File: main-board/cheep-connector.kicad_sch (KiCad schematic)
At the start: 5 parts, among them J1 Conn_02x16_Odd_Even, J2 Conn_02x16_Odd_Even, J3 Conn_02x16_Odd_Even, J4 Conn_02x16_Odd_Even, J5 Conn_02x16_Odd_Even

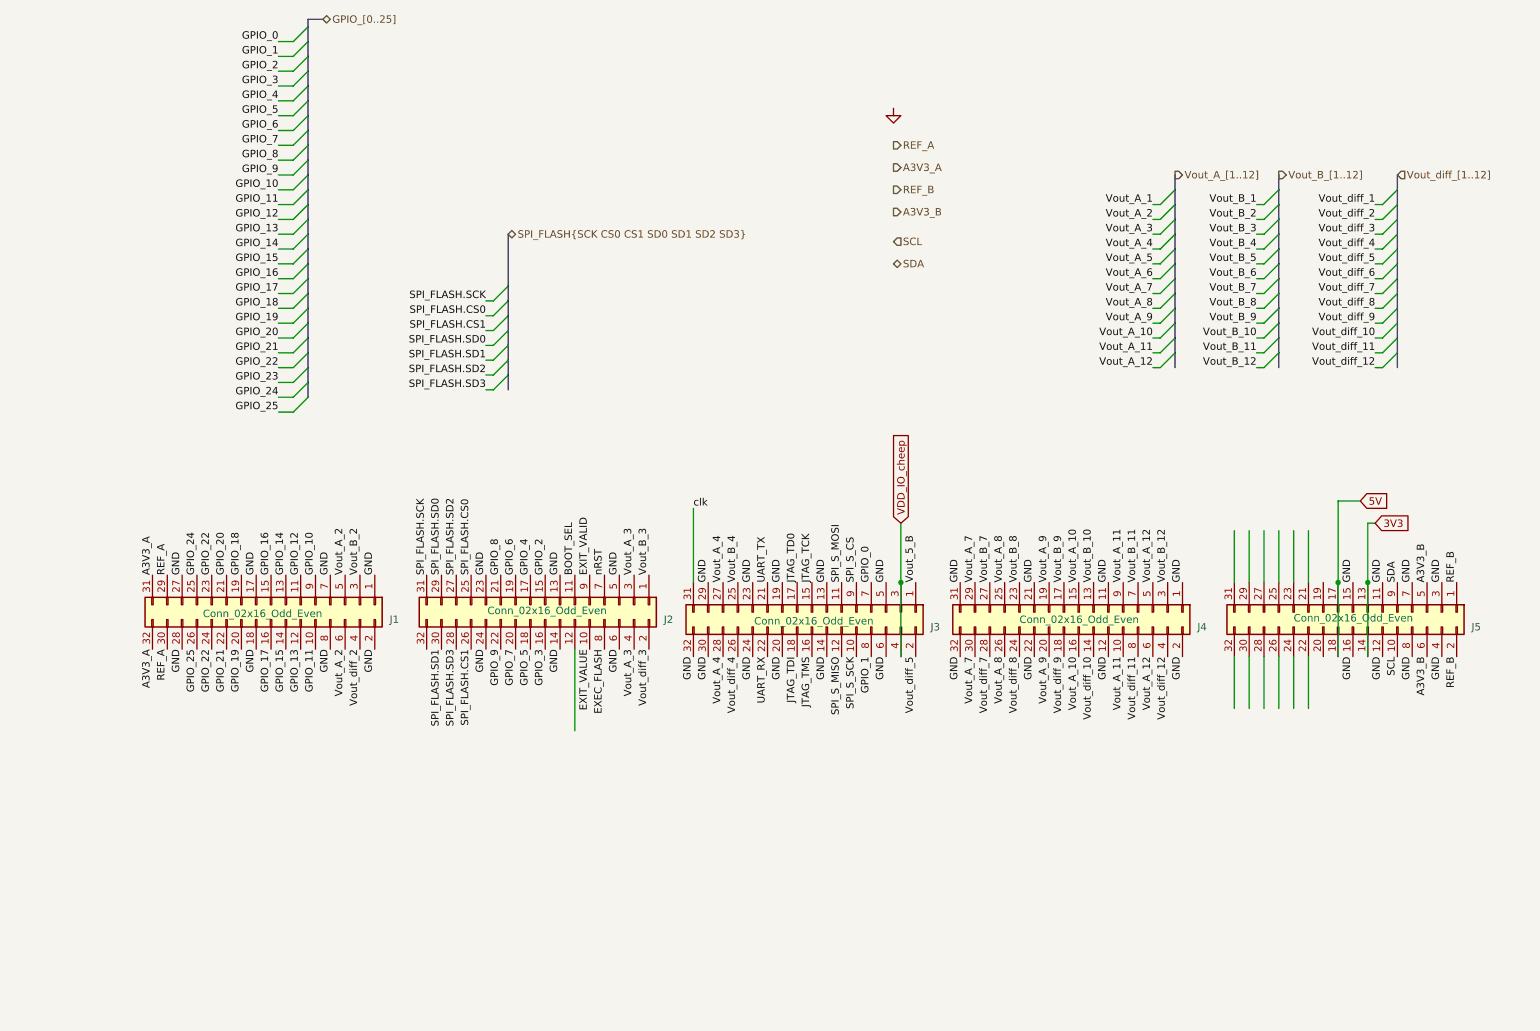
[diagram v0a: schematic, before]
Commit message: WIP: added i2c expanders and re-structuring i2c distributino
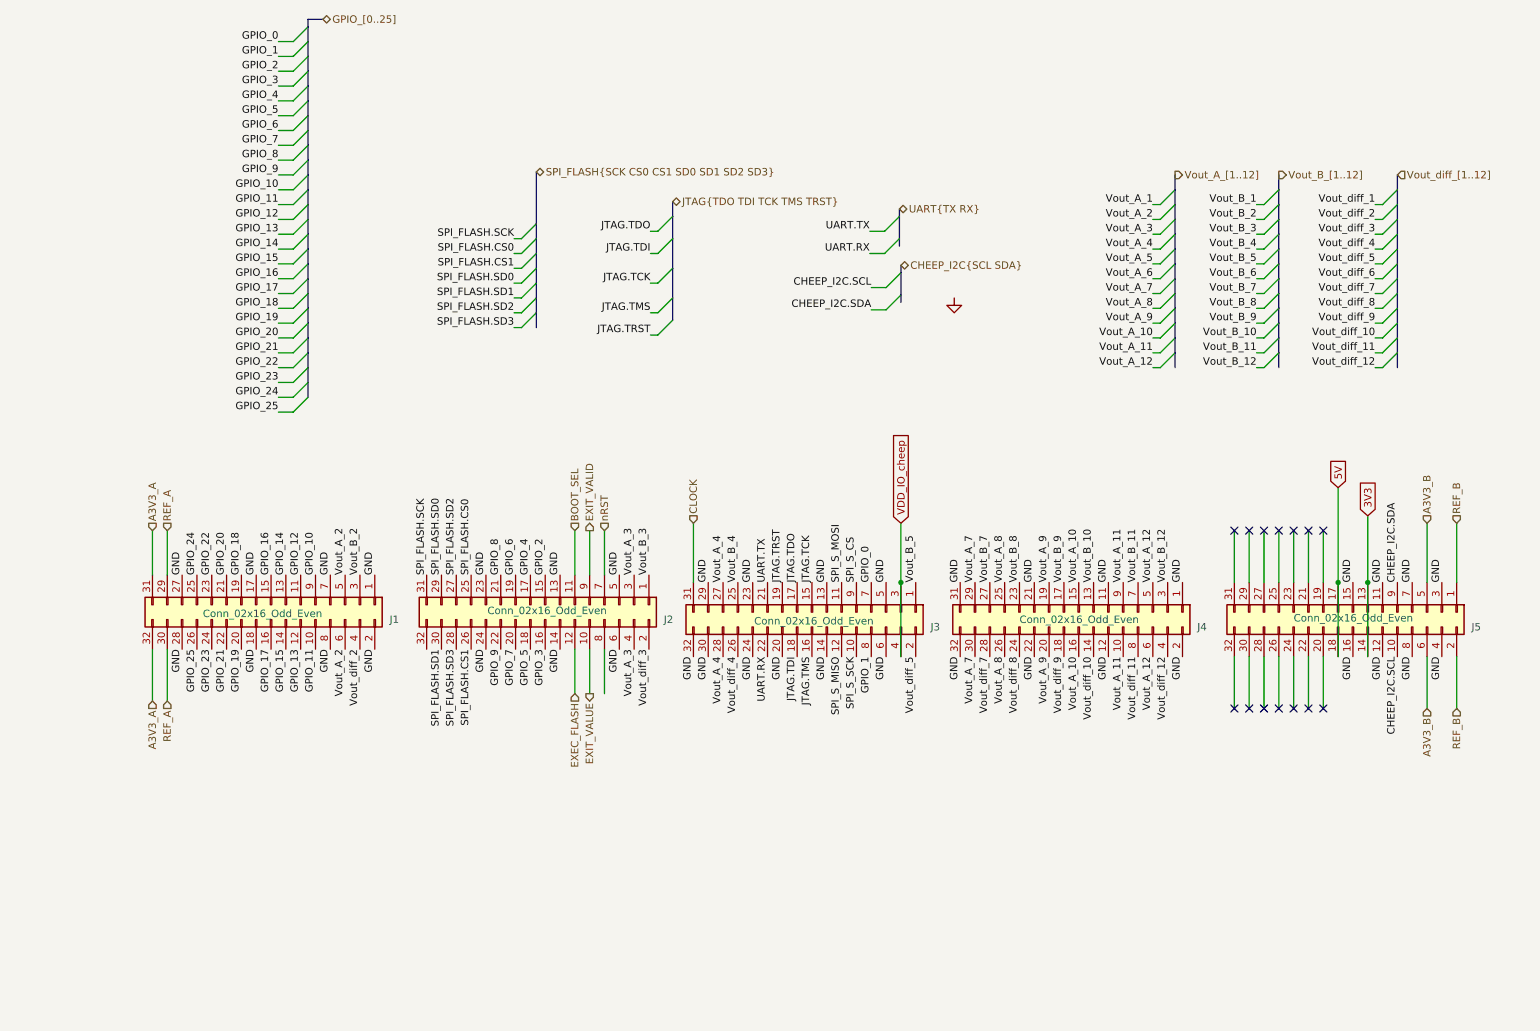
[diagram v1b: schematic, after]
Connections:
- net Vout_5_B is gone; now on net Vout_B_5: J3.1 (Pin_1)
- net EXEC_FLASH: now also J2.12 (Pin_12); no longer J2.8 (Pin_8)
- net GND: no longer J3.19 (Pin_19)
- net GPIO_22: no longer J1.24 (Pin_24)
- net GPIO_23: now also J1.24 (Pin_24)
- net JTAG_TCK renamed JTAG.TCK
- net JTAG_TD0 renamed JTAG.TDO
- net JTAG_TDI renamed JTAG.TDI
- net JTAG_TMS renamed JTAG.TMS
- net SCL renamed CHEEP_I2C.SCL
- net SDA renamed CHEEP_I2C.SDA
- net UART_RX renamed UART.RX
- net UART_TX renamed UART.TX
- net clk renamed CLOCK
- new net JTAG.TRST: J3.19 (Pin_19)
- no-connect marks 0 -> 14

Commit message: Routed all power signals and re-organized GPIOs
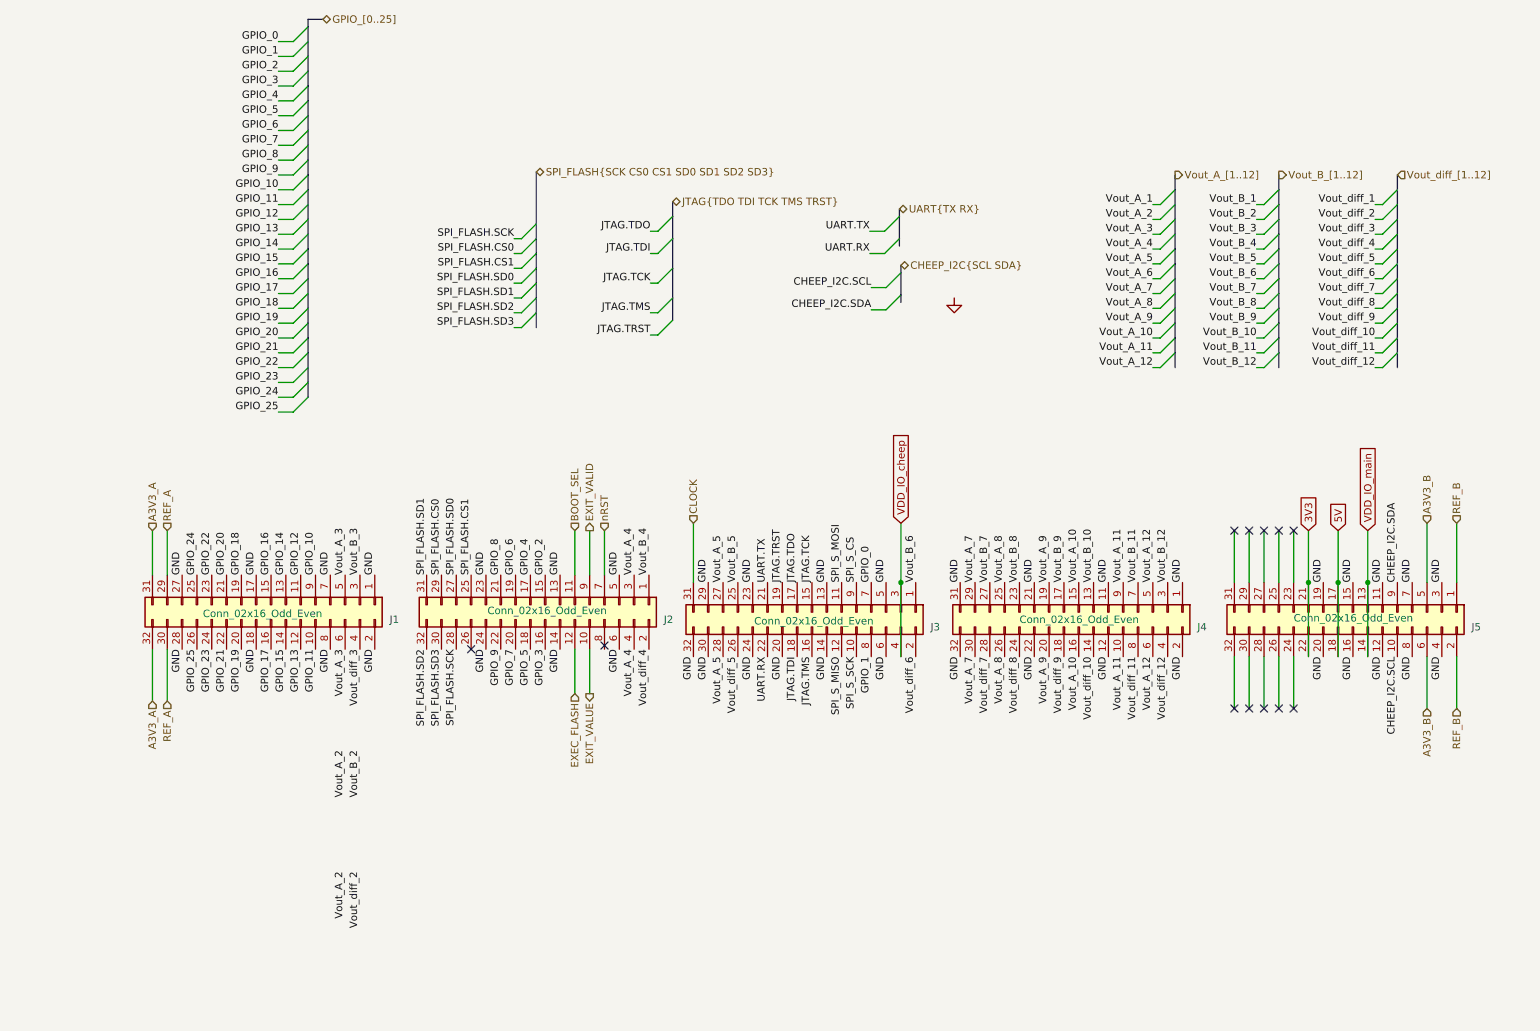
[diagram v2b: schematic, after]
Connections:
- net 3V3: now also J5.21 (Pin_21), J5.22 (Pin_22); no longer J5.13 (Pin_13), J5.14 (Pin_14)
- net GND: now also J5.19 (Pin_19), J5.20 (Pin_20)
- net SPI_FLASH.CS0: now also J2.29 (Pin_29); no longer J2.25 (Pin_25)
- net SPI_FLASH.CS1: now also J2.25 (Pin_25); no longer J2.26 (Pin_26)
- net SPI_FLASH.SCK: now also J2.28 (Pin_28); no longer J2.31 (Pin_31)
- net SPI_FLASH.SD0: now also J2.27 (Pin_27); no longer J2.29 (Pin_29)
- net SPI_FLASH.SD1: now also J2.31 (Pin_31); no longer J2.30 (Pin_30)
- net SPI_FLASH.SD2: now also J2.32 (Pin_32); no longer J2.27 (Pin_27)
- net SPI_FLASH.SD3: now also J2.30 (Pin_30); no longer J2.28 (Pin_28)
- net Vout_A_2: no longer J1.5 (Pin_5), J1.6 (Pin_6)
- net Vout_A_3: now also J1.5 (Pin_5), J1.6 (Pin_6); no longer J2.3 (Pin_3), J2.4 (Pin_4)
- net Vout_A_4: now also J2.3 (Pin_3), J2.4 (Pin_4); no longer J3.27 (Pin_27), J3.28 (Pin_28)
- net Vout_A_5: now also J3.27 (Pin_27), J3.28 (Pin_28)
- net Vout_B_2: no longer J1.3 (Pin_3)
- net Vout_B_3: now also J1.3 (Pin_3); no longer J2.1 (Pin_1)
- net Vout_B_4: now also J2.1 (Pin_1); no longer J3.25 (Pin_25)
- net Vout_B_5: now also J3.25 (Pin_25); no longer J3.1 (Pin_1)
- net Vout_B_6: now also J3.1 (Pin_1)
- net Vout_diff_2: no longer J1.4 (Pin_4)
- net Vout_diff_3: now also J1.4 (Pin_4); no longer J2.2 (Pin_2)
- net Vout_diff_4: now also J2.2 (Pin_2); no longer J3.26 (Pin_26)
- net Vout_diff_5: now also J3.26 (Pin_26); no longer J3.2 (Pin_2)
- net Vout_diff_6: now also J3.2 (Pin_2)
- new net VDD_IO_main: J5.13 (Pin_13), J5.14 (Pin_14)
- no-connect marks 14 -> 12

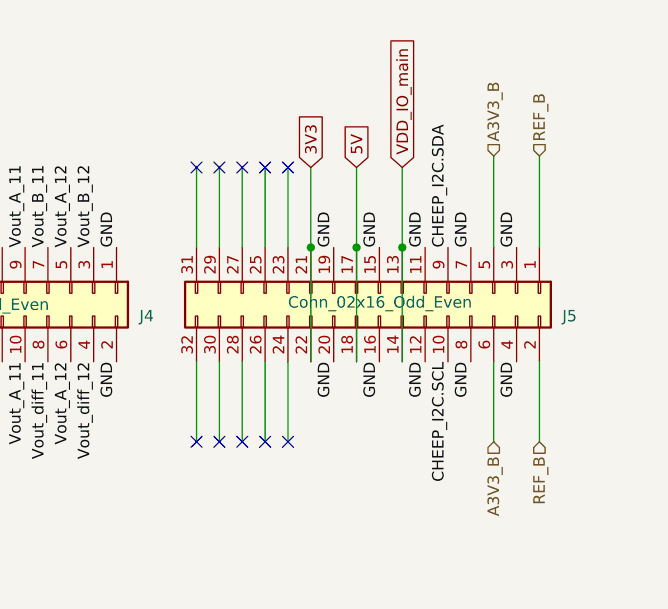
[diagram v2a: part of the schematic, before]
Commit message: rework main PCB: added USB-C, new connector symbol & footprints
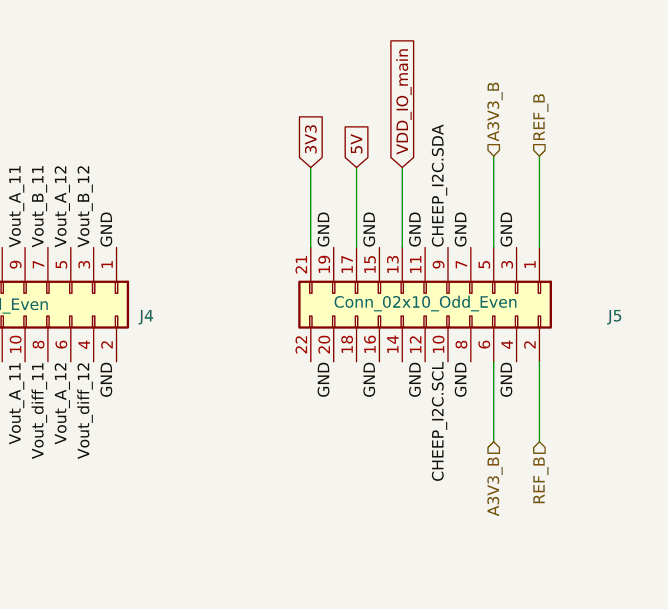
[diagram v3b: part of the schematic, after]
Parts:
- J5: value Conn_02x16_Odd_Even -> Conn_02x10_Odd_Even; symbol Connector_Generic:Conn_02x16_Odd_Even -> Connector_Generic:Conn_02x11_Odd_Even
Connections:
- net 3V3: no longer J5.22 (Pin_22)
- net 5V: no longer J5.18 (Pin_18)
- net VDD_IO_main: no longer J5.14 (Pin_14)
- no-connect marks 12 -> 2
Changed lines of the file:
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@@
 (kicad_sch
-	(version 20231120)
+	(version 20250114)
 	(generator "eeschema")
-	(generator_version "8.0")
+	(generator_version "9.0")
 	(paper "A4")
 	(junction
-		(at 240.03 119.38)
-		(diameter 0)
-		(color 0 0 0 0)
-	)
-	(junction
-		(at 234.95 119.38)
-		(diameter 0)
-		(color 0 0 0 0)
-	)
-	(junction
-		(at 245.11 119.38)
-		(diameter 0)
-		(color 0 0 0 0)
-	)
-	(junction
 		(at 165.1 119.38)
 		(diameter 0)
@@
 	)
 	(no_connect
-		(at 229.87 110.49)
-	)
-	(no_connect
 		(at 91.44 130.81)
 	)
 	(no_connect
-		(at 227.33 140.97)
-	)
-	(no_connect
-		(at 227.33 110.49)
-	)
-	(no_connect
 		(at 114.3 130.175)
 	)
-	(no_connect
-		(at 229.87 140.97)
-	)
-	(no_connect
-		(at 232.41 110.49)
-	)
-	(no_connect
-		(at 224.79 110.49)
-	)
-	(no_connect
-		(at 222.25 140.97)
-	)
-	(no_connect
-		(at 224.79 140.97)
-	)
-	(no_connect
-		(at 232.41 140.97)
-	)
-	(no_connect
-		(at 222.25 110.49)
-	)
 	(bus_entry
 		(at 60.96 64.77)
@@
 		)
 	)
-	(wire
-		(pts
-			(xy 234.95 119.38) (xy 234.95 132.08)
-		)
-		(stroke
-			(width 0)
-			(type default)
-		)
-	)
 	(bus
 		(pts
@@
 		)
 	)
-	(wire
-		(pts
-			(xy 222.25 132.08) (xy 222.25 140.97)
-		)
-		(stroke
-			(width 0)
-			(type default)
-		)
-	)
 	(bus
 		(pts
@@
 	(wire
 		(pts
-			(xy 240.03 119.38) (xy 240.03 132.08)
+			(xy 240.03 110.49) (xy 240.03 119.38)
 		)
 		(stroke
@@
 	(wire
 		(pts
-			(xy 229.87 132.08) (xy 229.87 140.97)
-		)
-		(stroke
-			(width 0)
-			(type default)
-		)
-	)
-	(wire
-		(pts
 			(xy 208.28 57.15) (xy 209.55 57.15)
 		)
@@
 	(wire
 		(pts
-			(xy 224.79 110.49) (xy 224.79 119.38)
-		)
-		(stroke
-			(width 0)
-			(type default)
-		)
-	)
-	(wire
-		(pts
 			(xy 246.38 57.15) (xy 247.65 57.15)
 		)
@@
 	(wire
 		(pts
-			(xy 245.11 119.38) (xy 245.11 132.08)
-		)
-		(stroke
-			(width 0)
-			(type default)
-		)
-	)
-	(wire
-		(pts
 			(xy 165.1 119.38) (xy 165.1 132.08)
 		)
@@
 		)
 	)
-	(wire
-		(pts
-			(xy 224.79 132.08) (xy 224.79 140.97)
-		)
-		(stroke
-			(width 0)
-			(type default)
-		)
-	)
 	(bus
 		(pts
@@
 	(wire
 		(pts
-			(xy 227.33 132.08) (xy 227.33 140.97)
-		)
-		(stroke
-			(width 0)
-			(type default)
-		)
-	)
-	(wire
-		(pts
 			(xy 159.766 62.992) (xy 162.306 62.992)
 		)
@@
 		)
 	)
-	(wire
-		(pts
-			(xy 229.87 110.49) (xy 229.87 119.38)
-		)
-		(stroke
-			(width 0)
-			(type default)
-		)
-	)
 	(bus
 		(pts
@@
 	(wire
 		(pts
-			(xy 232.41 132.08) (xy 232.41 140.97)
-		)
-		(stroke
-			(width 0)
-			(type default)
-		)
-	)
-	(wire
-		(pts
 			(xy 160.02 68.834) (xy 162.56 68.834)
 		)
@@
 	(wire
 		(pts
-			(xy 232.41 110.49) (xy 232.41 119.38)
-		)
-		(stroke
-			(width 0)
-			(type default)
-		)
-	)
-	(wire
-		(pts
 			(xy 260.35 140.97) (xy 260.35 132.08)
 		)
@@
 	(wire
 		(pts
-			(xy 227.33 110.49) (xy 227.33 119.38)
-		)
-		(stroke
-			(width 0)
-			(type default)
-		)
-	)
-	(wire
-		(pts
 			(xy 98.806 65.532) (xy 100.076 65.532)
 		)
@@
 	(wire
 		(pts
-			(xy 222.25 110.49) (xy 222.25 119.38)
-		)
-		(stroke
-			(width 0)
-			(type default)
-		)
-	)
-	(wire
-		(pts
-			(xy 240.03 110.49) (xy 240.03 119.38)
-		)
-		(stroke
-			(width 0)
-			(type default)
-		)
-	)
-	(wire
-		(pts
 			(xy 122.174 73.152) (xy 123.444 73.152)
 		)
@@
 	)
 	(symbol
-		(lib_id "Connector_Generic:Conn_02x16_Odd_Even")
-		(at 242.57 124.46 270)
+		(lib_id "Connector_Generic:Conn_02x11_Odd_Even")
+		(at 247.65 124.46 270)
 		(unit 1)
 		(exclude_from_sim no)
@@
 		(dnp no)
 		(property "Reference" "J5"
-			(at 262.89 127.0001 90)
+			(at 267.97 127.0001 90)
 			(effects
 				(font
@@
 			)
 		)
-		(property "Value" "Conn_02x16_Odd_Even"
-			(at 232.41 125.476 90)
+		(property "Value" "Conn_02x10_Odd_Even"
+			(at 237.49 125.476 90)
 			(effects
 				(font
@@
 		)
 		(property "Footprint" ""
-			(at 242.57 124.46 0)
+			(at 247.65 124.46 0)
 			(effects
 				(font
@@
 		)
 		(property "Datasheet" "~"
-			(at 242.57 124.46 0)
+			(at 247.65 124.46 0)
 			(effects
 				(font
@@
 			)
 		)
-		(property "Description" "Generic connector, double row, 02x16, odd/even pin numbering scheme (row 1 odd numbers, row 2 even numbers), script generated (kicad-library-utils/schlib/autogen/connector/)"
-			(at 242.57 124.46 0)
+		(property "Description" "Generic connector, double row, 02x11, odd/even pin numbering scheme (row 1 odd numbers, row 2 even numbers), script generated (kicad-library-utils/schlib/autogen/connector/)"
+			(at 247.65 124.46 0)
 			(effects
 				(font
@@
 		(pin "19"
 		)
-		(pin "32"
-		)
 		(pin "18"
 		)
@@
 		(pin "3"
 		)
-		(pin "31"
-		)
 		(pin "4"
 		)
-		(pin "27"
-		)
 		(pin "6"
 		)
 		(pin "7"
 		)
-		(pin "28"
-		)
 		(pin "5"
 		)
-		(pin "24"
-		)
 		(pin "11"
 		)
 		(pin "9"
 		)
-		(pin "30"
-		)
-		(pin "25"
-		)
-		(pin "29"
-		)
 		(pin "12"
 		)
@@
 		(pin "10"
 		)
-		(pin "23"
-		)
-		(pin "26"
-		)
 		(pin "1"
 		)
@@
 		(pin "14"
 		)
-		(pin "22"
-		)
 		(pin "15"
 		)
 		(pin "21"
 		)
+		(pin "22"
+		)
 		(instances
